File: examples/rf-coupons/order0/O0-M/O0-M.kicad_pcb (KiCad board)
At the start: 4 copper layers, 141.1 x 117.2 mm, 79 parts, among them X19 Anchor, X21 Anchor, X42 Anchor, X53 Anchor

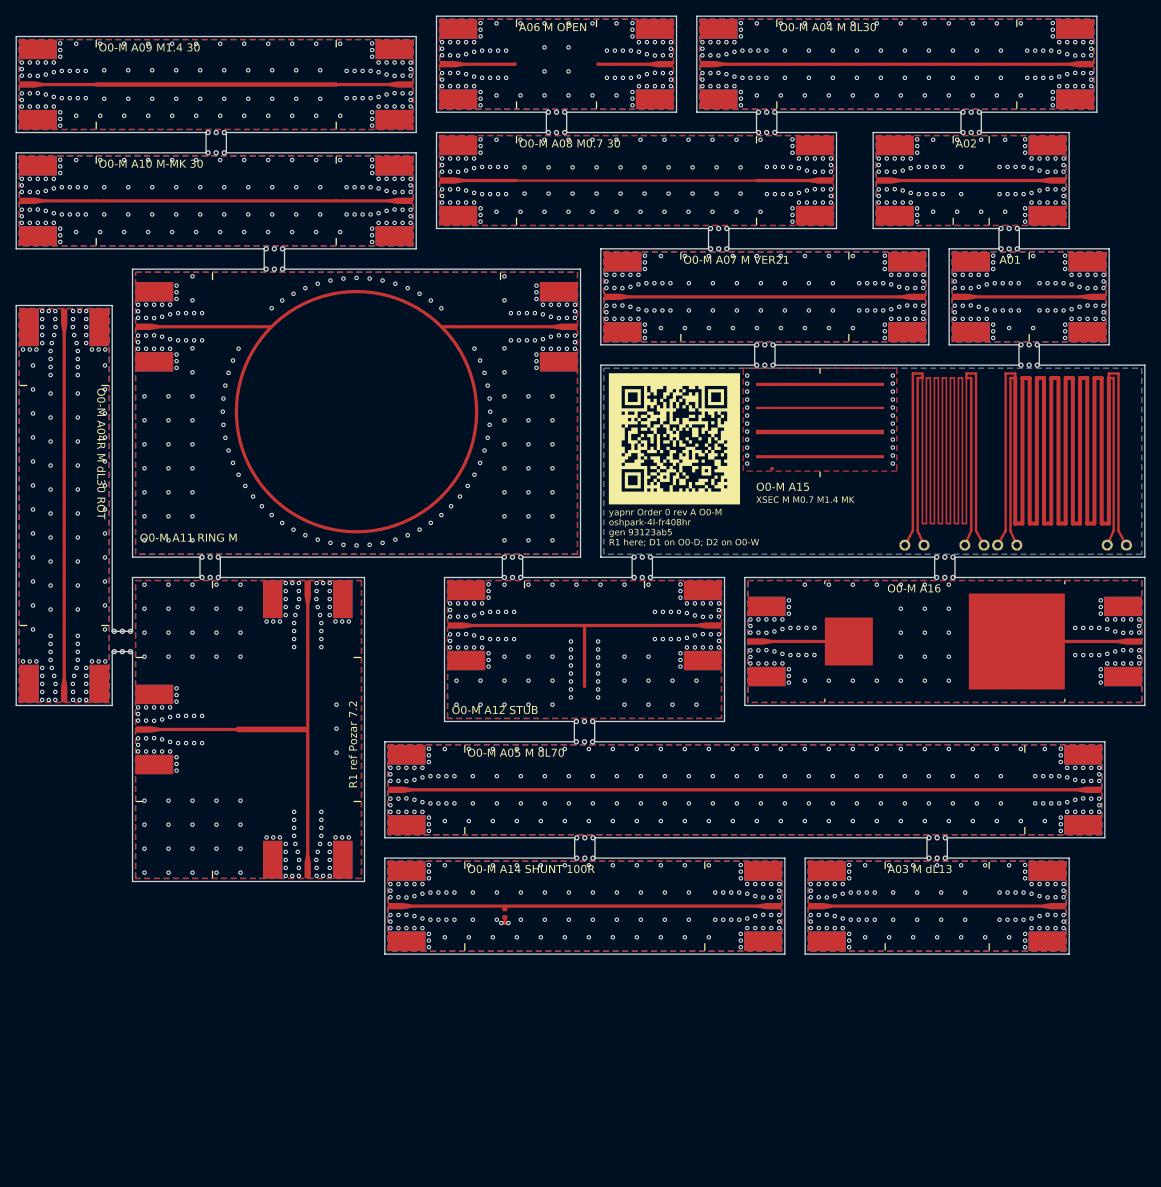
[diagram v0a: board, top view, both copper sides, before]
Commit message: Order 0: the uploads and predictions regenerated after the review
examples/rf-coupons/order0: generated from 73fe6527 (the tag carries it); KiCad
DRC under OSH Park's 4-layer rules 0 violations / 0 unconnected on all three.
`yapnr fab check` (oshpark-4l, oshpark-4l-fr408hr): O0-M 0 errors; O0-W and
O0-D stop on FAB-PLACEHOLDER until D2 and D1 are in (by design); warnings as
before (NPTH in the merged drill file; 1.511 mm of published layers):

- O0-M 120.1 x 144.3 mm, 26.9 sq in, 33 SMAs per copy, 32 tabs;
- O0-W 57.5 x 131.2 mm, 11.7 sq in, 16 SMAs, 15 tabs;
- O0-D 90.6 x 51.5 mm, 7.2 sq in, 12 SMAs, 9 tabs (A20 added).

Every stick has two or more tabs, all on edges without a launch; no plane via
under a silkscreen glyph; no mask web under 0.1 mm; the QR decodes from the
silkscreen render.

Predictions: the coupons on FR408HR and EM528 with the review's roughness
prior, the junction-corrected ring and stub (A12 notch 5.500 GHz FR408HR,
5.388 GHz EM528; A11 1.924 / 5.793 GHz), scalars.json and lines.csv. Boards A
and B regenerated (mask-opening anchors only; DRC unchanged).

docs/rf/order0: sizes and costs, R1/R1t as drawn, the renormalization to the
solver's port impedance (review H3), the C-pad method (M3), the loss basis
(M4), the scalars (L1), the sha256 rule (F9), the connector-fit pre-check, the
mask web note (L2), and the D1/D2 pages with the board around each window.

Co-Authored-By: Claude Opus 5.5 <noreply@anthropic.com>
Claude-Session: https://claude.ai/code/session_01NY8rMuBH8hTFjkoZyuqNZ7
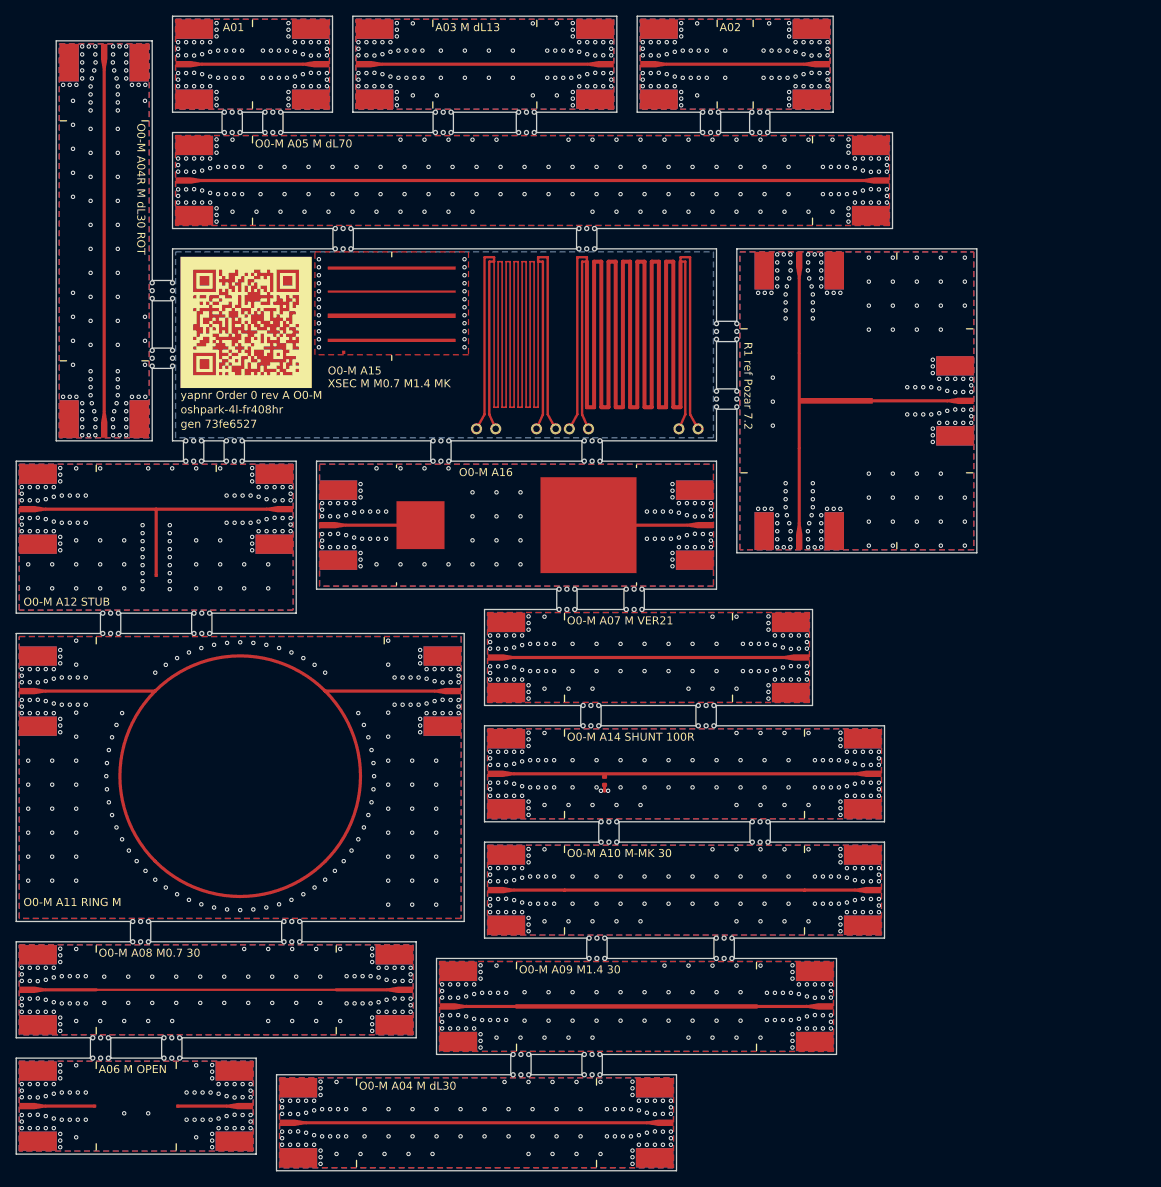
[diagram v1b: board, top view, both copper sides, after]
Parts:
- added MO_A11LJ: MaskOpening, MaskOpening, F.Cu at (34.4, 100.7)
- added MO_A11RJ: MaskOpening, MaskOpening, F.Cu at (55.8, 100.7)
- moved MO_A04 151.1 mm to (55.0, 157.1)
- moved JA04E 142.4 mm to (102.5, 158.3)
- moved JA04W 142.4 mm to (52.5, 158.3)
- moved MO_A06R 142.1 mm to (39.0, 155.0)
- moved JA06E 140.4 mm to (50.0, 156.2)
- moved JA06W 140.4 mm to (20.0, 156.2)
- moved X19 140.4 mm to (29.8, 156.2)
- moved X21 140.4 mm to (40.2, 156.2)
- moved MO_A06L 139.9 mm to (22.5, 155.0)
- moved MO_A03 127.7 mm to (64.6, 24.8)
- moved JA09E 126.7 mm to (122.5, 143.8)
- moved JA09W 126.7 mm to (72.5, 143.8)
- moved MO_A08 125.0 mm to (22.5, 140.5)
- moved JA03E 119.5 mm to (95.1, 26.0)
- moved JA03W 119.5 mm to (62.1, 26.0)
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- renumbered X42 to X44, X53 to X55
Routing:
- net RF_A12: track 35.2 -> 35.9 mm
- net GND_A14: vias 118 -> 108
- net GND_R1: vias 151 -> 149
- net GND_A16: vias 95 -> 92
- net GND_A12: vias 118 -> 119
- net GND_A11: vias 180 -> 177
- net GND_A10: vias 116 -> 107
- net GND_A09: vias 116 -> 107
- net GND_A08: vias 116 -> 107
- net GND_A07: vias 104 -> 95
- net GND_A06: vias 88 -> 78
- net GND_A05: vias 170 -> 158
- net GND_A04R: vias 116 -> 105
- net GND_A04: vias 116 -> 107
- net GND_A03: vias 94 -> 87
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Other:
- board size 141.1 x 117.2 mm -> 120.1 x 144.3 mm
- board text added: "O0-M A01"
- board text added: "O0-M A02"
- board text added: "O0-M A03"
- board text added: "O0-M A04"
- board text added: "O0-M A04R"
- board text added: "O0-M A05"
- board text added: "O0-M A06"
- board text added: "O0-M A07"
- board text added: "O0-M A08"
- board text added: "O0-M A09"
- board text added: "O0-M A10"
- board text added: "O0-M A11"
- board text added: "O0-M A12"
- board text added: "O0-M A14"
- board text added: "O0-M R1"
- board text added: "gen 73fe6527"
- board text removed: "A03"
- board text removed: "A04"
- board text removed: "A04R"
- board text removed: "A05"
- board text removed: "A06"
- board text removed: "A07"
- board text removed: "A08"
- board text removed: "A09"
- board text removed: "A10"
- board text removed: "A11"
- board text removed: "A12"
- board text removed: "A14"
- board text removed: "A15"
- board text removed: "A16"
- board text removed: "R1"
- board text removed: "R1 here; D1 on O0-D; D2 on O0-W"
- board text removed: "gen 93123ab5"
